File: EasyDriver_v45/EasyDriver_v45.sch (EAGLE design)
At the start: 43 parts, among them IC1 A3967SLB, IC2 V_REG_317SMD

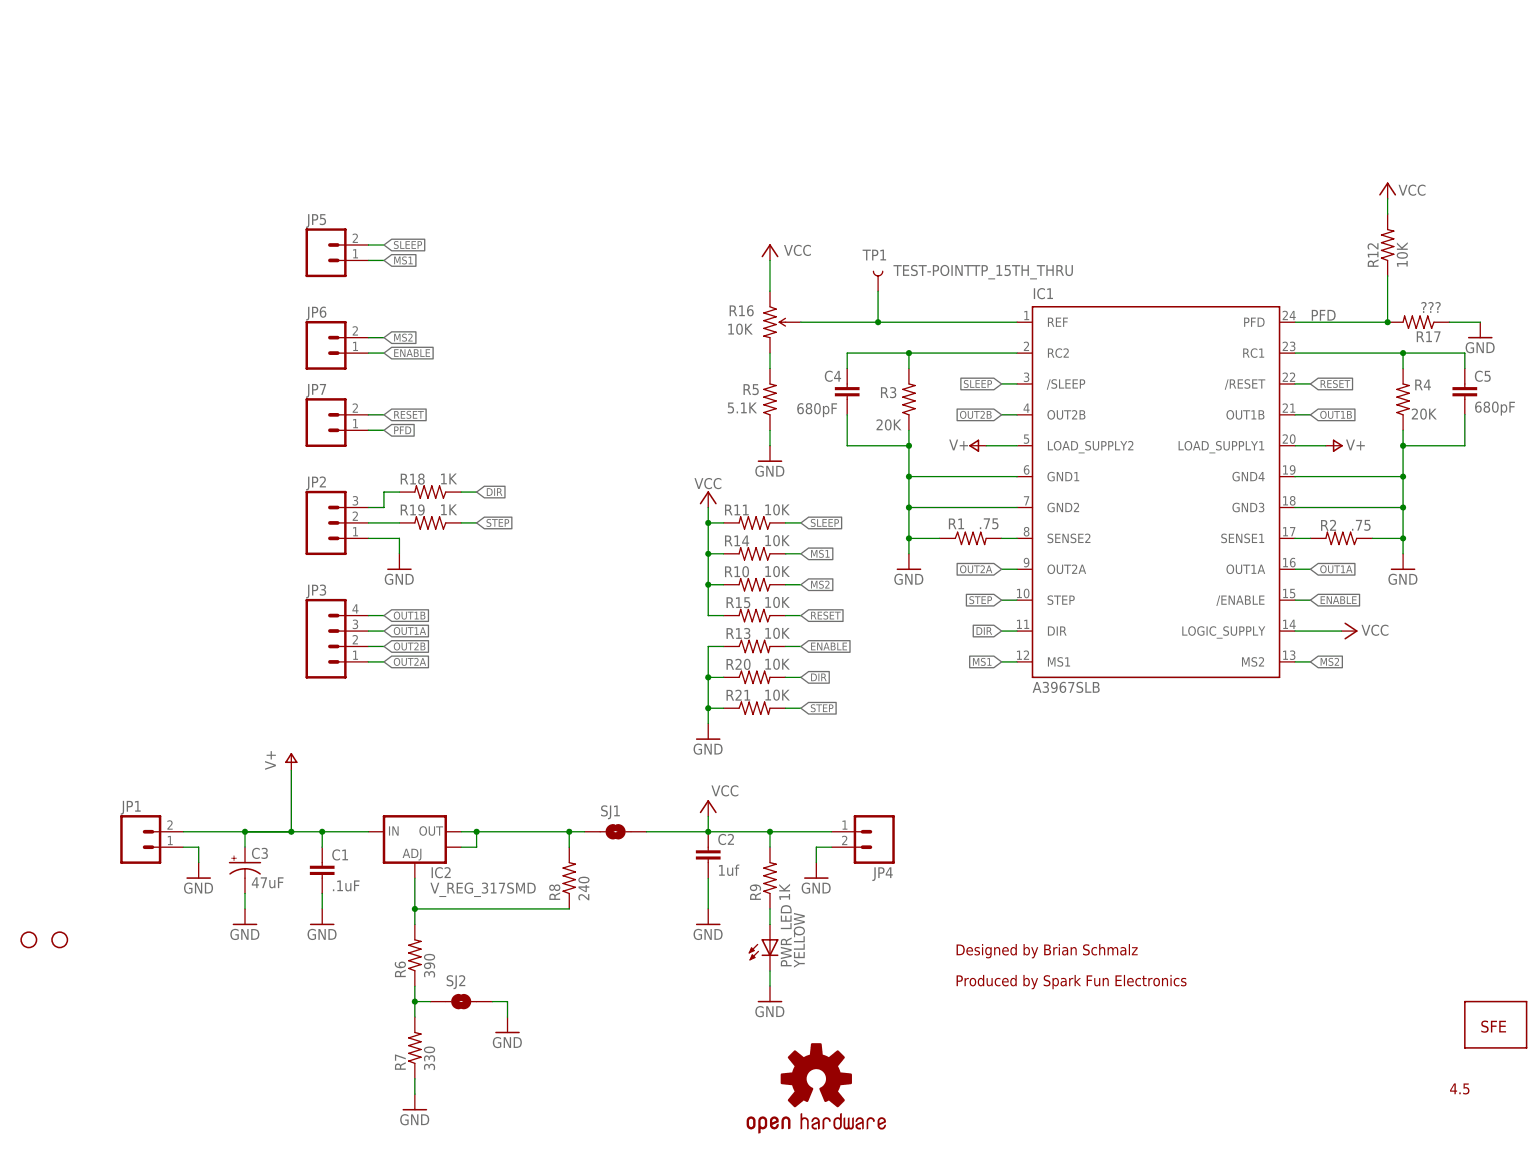
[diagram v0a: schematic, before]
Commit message: * Made TP1 bigger, and no longer covered with solder mask * Switched R5 to 2.4K Ohms to allow Vref down to 1V into driver * Set R17 to 6.8K to allow PFD input to select 'mixed-decay' mode * Swapped location of STEP and DIR series resistors so that pull downs now happen before series Rs. * Suggest SparkFun adjust current limit pot to 2V (measured by TP1) at final test.
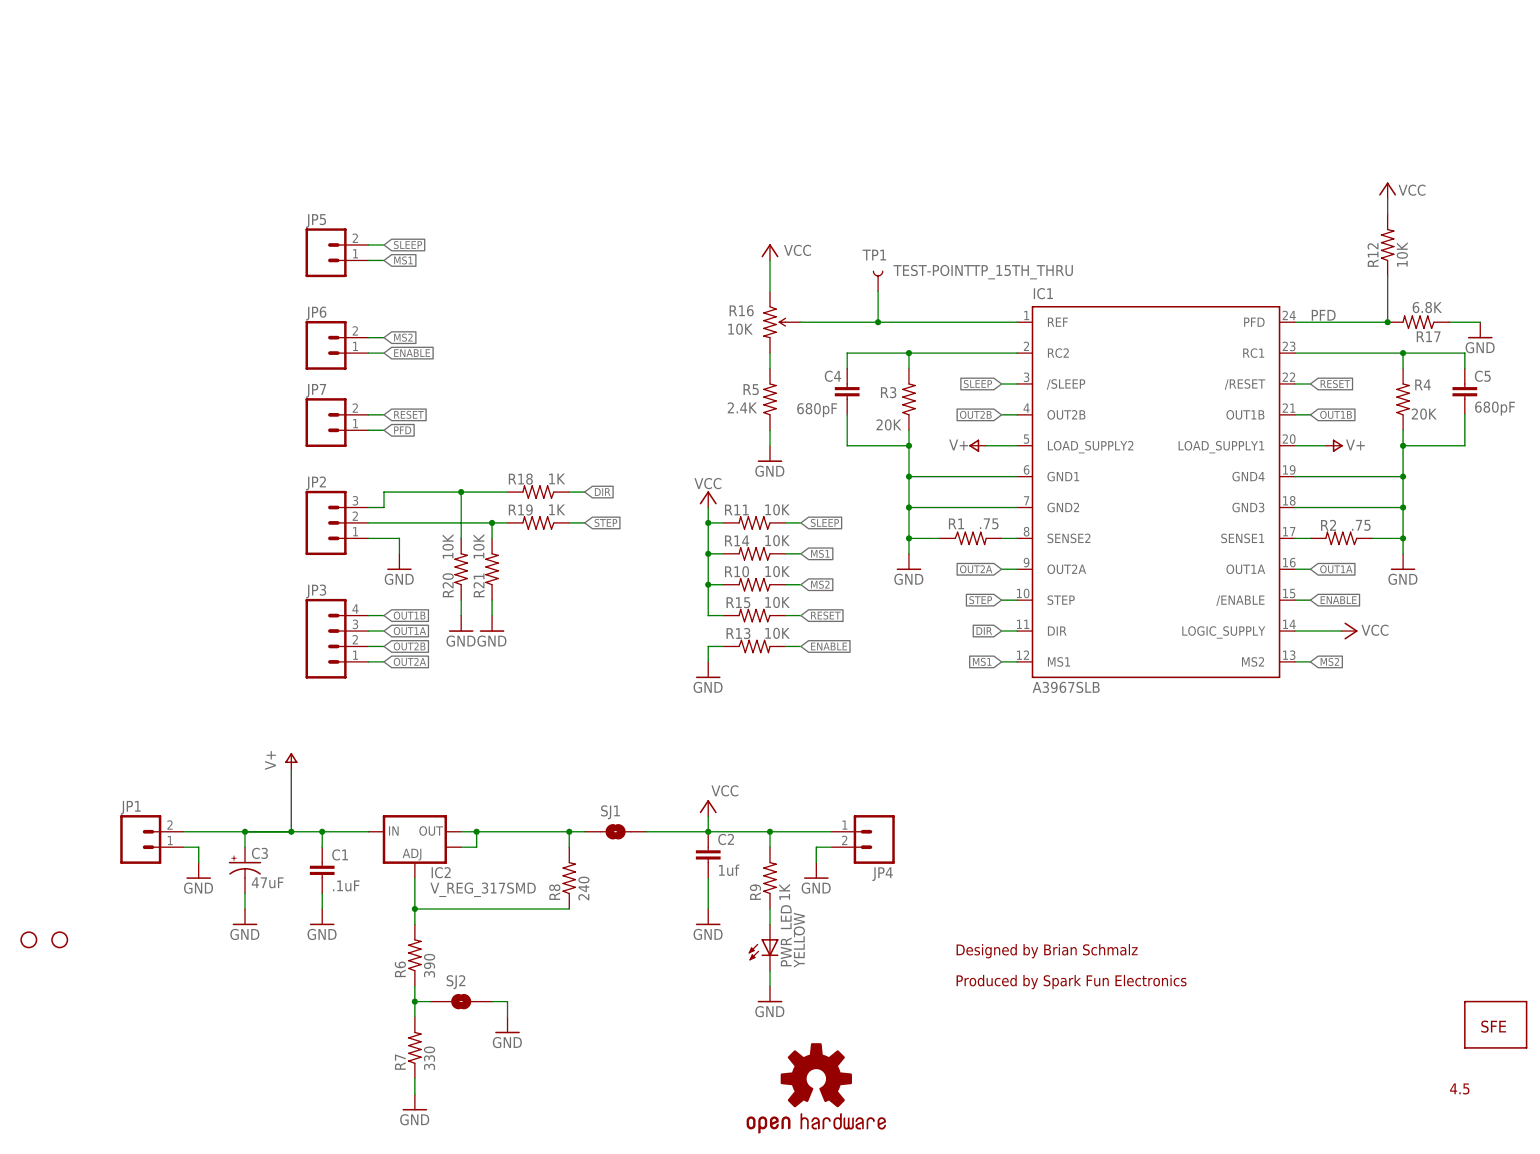
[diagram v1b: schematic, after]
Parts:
- R17: value ??? -> 6.8K
- R5: value 5.1K -> 2.4K
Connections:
- net N$12 renamed VREF
- net DIR: no longer R20.2
- net DIR_IN: now also R20.2
- net STEP: no longer R21.2
- net STEP_IN: now also R21.2
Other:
- note added: "Added series resistors and pull downs on STEP/DIR Updated pot fooprint Made bottom layer GND rather than VCC Updated to latest SparkFun footprints Swithed from CC BY 3.0 to CC BY-SA 3.0 license Fixed pot silkscreen direction R5 now 2.5K Ohms to get down to 1V on Vref R17 now 6.8K to set PDF to 'mixed-decay' mode"
- note added: "Set R16 to 2.0V at factory = 333mA/phase"
- note added: "Set for 'mixed-decay' mode."
- note removed: "Added series resistors and pull downs on STEP/DIR Updated pot fooprint Made bottom layer GND rather than VCC Updated to latest SparkFun footprints Swithed from CC BY 3.0 to CC BY-SA 3.0 license Fixed pot silkscreen direction"
- note removed: "Change R12 and add in"
- note removed: "NOPOP"
- note removed: "R17 to create any voltage"
- note removed: "See datasheet"
- note removed: "on PFD for best high"
- note removed: "speed performance."
- moved on the sheet: R18, R19, R20, R21

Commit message: Based on SparkFun feedback * Replaced frame with newest version from SparkFun library * Replaced VCC symbol with newest version from SparkFun library * Move components so that keepout area around mounding holes is honored.
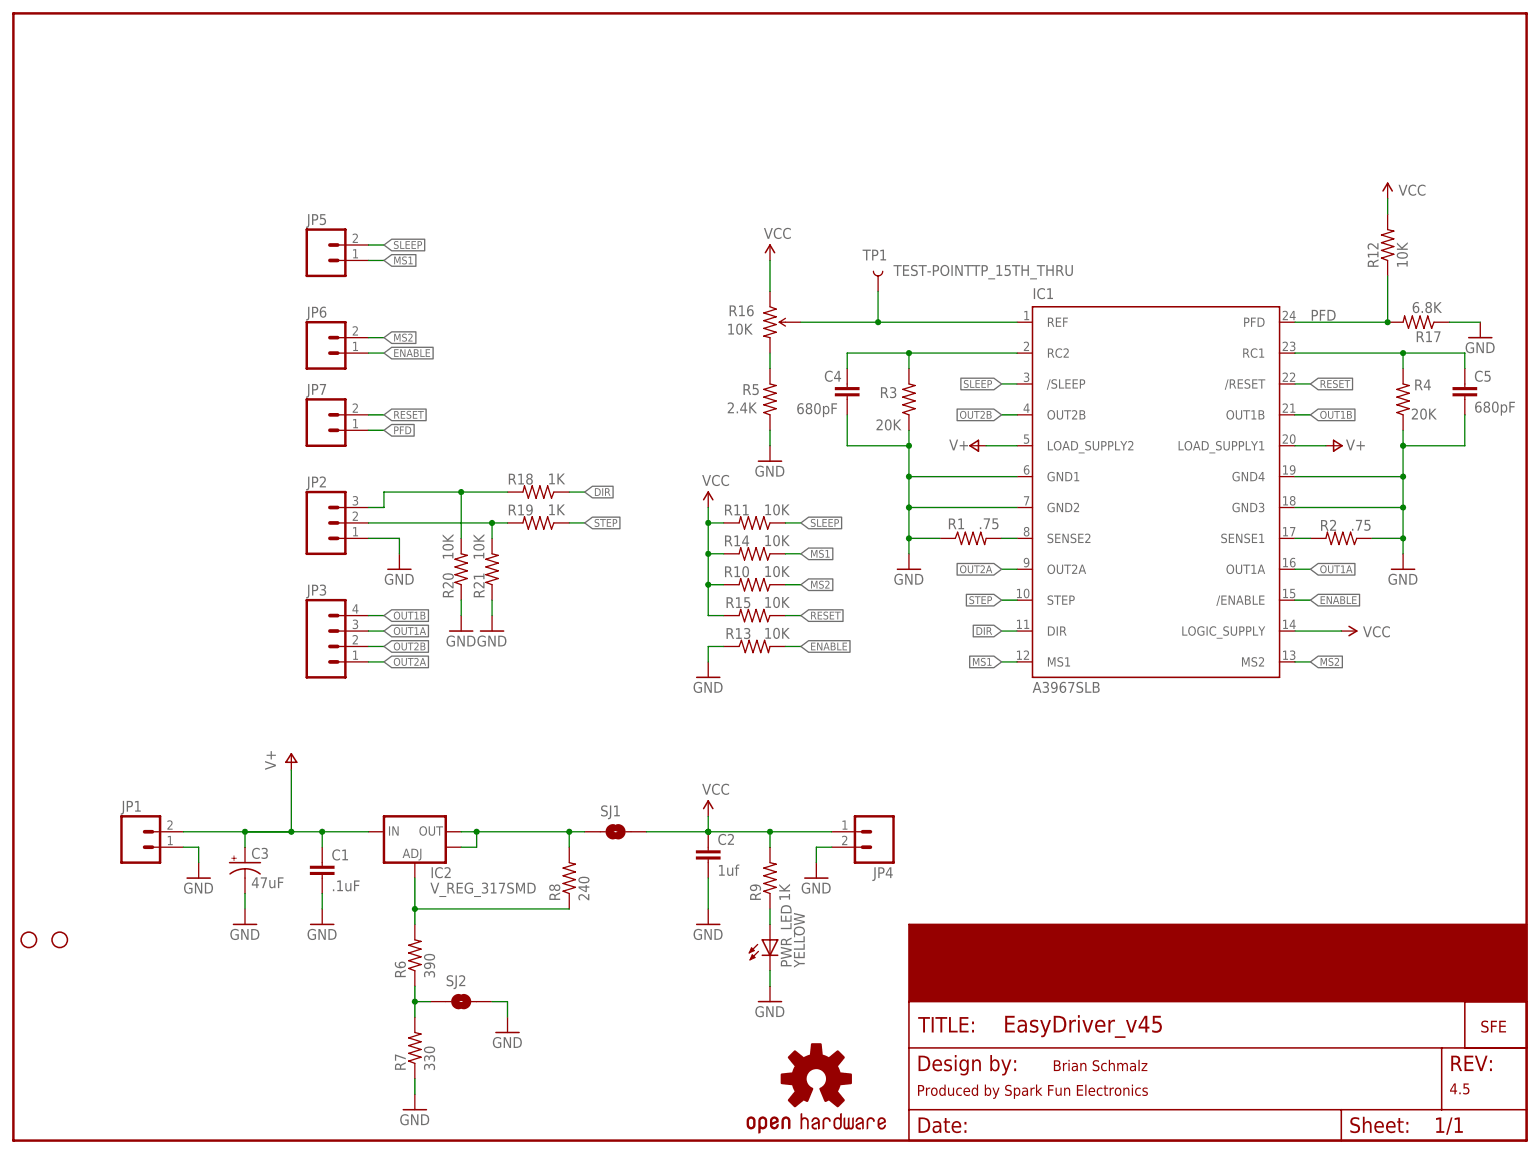
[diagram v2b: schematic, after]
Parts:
- added FRAME2: FRAME-LETTER, SparkFun-Aesthetics:FRAME-LETTER
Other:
- note added: "Brian Schmalz"
- note removed: "Designed by Brian Schmalz"
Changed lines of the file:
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@@
 <?xml version="1.0" encoding="utf-8"?>
 <!DOCTYPE eagle SYSTEM "eagle.dtd">
-<eagle version="6.4">
+<eagle version="6.5.0">
 <drawing>
 <settings>
@@
 <part name="GND2" library="supply1" deviceset="GND" device=""/>
 <part name="GND3" library="supply1" deviceset="GND" device=""/>
-<part name="P+3" library="supply1" deviceset="+5V" device="" value="VCC"/>
 <part name="GND6" library="supply1" deviceset="GND" device=""/>
-<part name="P+5" library="supply1" deviceset="+5V" device="" value="VCC"/>
 <part name="R1" library="SparkFun-Resistors" deviceset="RESISTOR" device="0805-RES" value=".75"/>
 <part name="R2" library="SparkFun-Resistors" deviceset="RESISTOR" device="0805-RES" value=".75"/>
@@
 <part name="R3" library="SparkFun-Resistors" deviceset="RESISTOR" device="0603" value="20K"/>
 <part name="C2" library="SparkFun-Capacitors" deviceset="CAP" device="0603-CAP" value="1uf"/>
-<part name="P+4" library="supply1" deviceset="+5V" device="" value="VCC"/>
 <part name="C3" library="rcl" deviceset="CPOL-US" device="D" value="47uF"/>
 <part name="P+10" library="supply1" deviceset="V+" device=""/>
 <part name="P+11" library="supply1" deviceset="V+" device=""/>
 <part name="MOT_PWR" library="supply1" deviceset="V+" device=""/>
-<part name="P+13" library="supply1" deviceset="+5V" device="" value="VCC"/>
 <part name="GND1" library="supply1" deviceset="GND" device=""/>
 <part name="R5" library="SparkFun-Resistors" deviceset="RESISTOR" device="0603" value="2.4K"/>
-<part name="FRAME1" library="SparkFun" deviceset="FRAME-LETTER" device=""/>
 <part name="R6" library="SparkFun-Resistors" deviceset="RESISTOR" device="0603" value="390"/>
 <part name="R8" library="SparkFun-Resistors" deviceset="RESISTOR" device="0603" value="240"/>
@@
 <part name="R15" library="SparkFun-Resistors" deviceset="RESISTOR" device="0603" value="10K"/>
 <part name="R10" library="SparkFun-Resistors" deviceset="RESISTOR" device="0603" value="10K"/>
-<part name="P+1" library="supply1" deviceset="+5V" device="" value="VCC"/>
 <part name="C4" library="SparkFun-Capacitors" deviceset="CAP" device="0603-CAP" value="680pF"/>
 <part name="C5" library="SparkFun-Capacitors" deviceset="CAP" device="0603-CAP" value="680pF"/>
@@
 <part name="GND8" library="supply1" deviceset="GND" device=""/>
 <part name="GND16" library="supply1" deviceset="GND" device=""/>
+<part name="FRAME2" library="SparkFun-Aesthetics" deviceset="FRAME-LETTER" device=""/>
+<part name="SUPPLY1" library="SparkFun-Aesthetics" deviceset="VCC" device=""/>
+<part name="SUPPLY2" library="SparkFun-Aesthetics" deviceset="VCC" device=""/>
+<part name="SUPPLY3" library="SparkFun-Aesthetics" deviceset="VCC" device=""/>
+<part name="SUPPLY4" library="SparkFun-Aesthetics" deviceset="VCC" device=""/>
+<part name="SUPPLY5" library="SparkFun-Aesthetics" deviceset="VCC" device=""/>
 </parts>
 <sheets>
 <sheet>
 <plain>
-<text x="154.94" y="30.48" size="1.778" layer="94">Designed by Brian Schmalz</text>
-<text x="154.94" y="25.4" size="1.778" layer="94">Produced by Spark Fun Electronics</text>
+<text x="170.942" y="11.43" size="1.778" layer="94">Brian Schmalz</text>
+<text x="148.59" y="7.366" size="1.778" layer="94">Produced by Spark Fun Electronics</text>
 <text x="134.62" y="55.88" size="1.778" layer="98">Vcc output
 Max 70mA used
@@
 <text x="116.84" y="154.94" size="1.778" layer="98">Max Coil Current(in Amps) = Vref(in Volts)/6</text>
 <text x="116.84" y="152.4" size="1.778" layer="98">Set R16 to 2.0V at factory = 333mA/phase</text>
+<rectangle x1="147.32" y1="22.86" x2="248.92" y2="35.56" layer="94"/>
 </plain>
 <instances>
@@
 <instance part="GND2" gate="1" x="147.32" y="93.98"/>
 <instance part="GND3" gate="1" x="228.6" y="93.98"/>
-<instance part="P+3" gate="1" x="220.98" y="83.82" smashed="yes" rot="R270">
-<attribute name="VALUE" x="221.742" y="83.058" size="1.778" layer="96"/>
-</instance>
 <instance part="GND6" gate="1" x="114.3" y="76.2"/>
-<instance part="P+5" gate="1" x="114.3" y="106.68" smashed="yes">
-<attribute name="VALUE" x="112.014" y="107.188" size="1.778" layer="96"/>
-</instance>
 <instance part="R1" gate="G$1" x="157.48" y="99.06" smashed="yes">
 <attribute name="NAME" x="153.67" y="100.5586" size="1.778" layer="95"/>
@@
 </instance>
 <instance part="C2" gate="G$1" x="114.3" y="45.72"/>
-<instance part="P+4" gate="1" x="114.3" y="55.88" smashed="yes">
-<attribute name="VALUE" x="114.808" y="56.642" size="1.778" layer="96"/>
-</instance>
 <instance part="C3" gate="G$1" x="38.1" y="45.72"/>
 <instance part="P+10" gate="1" x="157.48" y="114.3" smashed="yes" rot="R90">
@@
 </instance>
 <instance part="MOT_PWR" gate="1" x="45.72" y="63.5"/>
-<instance part="P+13" gate="1" x="226.06" y="157.48" smashed="yes">
-<attribute name="VALUE" x="227.838" y="155.448" size="1.778" layer="96"/>
-</instance>
 <instance part="GND1" gate="1" x="124.46" y="111.76"/>
 <instance part="R5" gate="G$1" x="124.46" y="121.92" smashed="yes" rot="R90">
@@
 <attribute name="VALUE" x="117.348" y="119.634" size="1.778" layer="96"/>
 </instance>
-<instance part="FRAME1" gate="G$1" x="0" y="0"/>
-<instance part="FRAME1" gate="G$2" x="147.32" y="0"/>
 <instance part="R6" gate="G$1" x="66.04" y="30.48" rot="R90"/>
 <instance part="R8" gate="G$1" x="91.44" y="43.18" rot="R90"/>
@@
 <attribute name="NAME" x="116.84" y="92.6846" size="1.778" layer="95"/>
 <attribute name="VALUE" x="123.444" y="92.71" size="1.778" layer="96"/>
-</instance>
-<instance part="P+1" gate="1" x="124.46" y="147.32" smashed="yes">
-<attribute name="VALUE" x="126.746" y="145.542" size="1.778" layer="96"/>
 </instance>
 <instance part="C4" gate="G$1" x="137.16" y="121.92" smashed="yes">
@@
 <instance part="GND8" gate="1" x="73.66" y="83.82"/>
 <instance part="GND16" gate="1" x="78.74" y="83.82"/>
+<instance part="FRAME2" gate="G$1" x="0" y="0"/>
+<instance part="FRAME2" gate="G$2" x="147.32" y="0"/>
+<instance part="SUPPLY1" gate="G$1" x="114.3" y="53.34"/>
+<instance part="SUPPLY2" gate="G$1" x="124.46" y="144.78"/>
+<instance part="SUPPLY3" gate="G$1" x="226.06" y="154.94" smashed="yes">
+<attribute name="VALUE" x="227.838" y="155.448" size="1.778" layer="96"/>
+</instance>
+<instance part="SUPPLY4" gate="G$1" x="218.44" y="83.82" smashed="yes" rot="R270">
+<attribute name="VALUE" x="221.996" y="82.804" size="1.778" layer="96"/>
+</instance>
+<instance part="SUPPLY5" gate="G$1" x="114.3" y="104.14"/>
 </instances>
 <busses>
@@
 <segment>
 <wire x1="226.06" y1="152.4" x2="226.06" y2="154.94" width="0.1524" layer="91"/>
-<pinref part="P+13" gate="1" pin="+5V"/>
 <pinref part="R12" gate="G$1" pin="2"/>
+<pinref part="SUPPLY3" gate="G$1" pin="VCC"/>
 </segment>
 <segment>
 <wire x1="210.82" y1="83.82" x2="218.44" y2="83.82" width="0.1524" layer="91"/>
 <pinref part="IC1" gate="G$1" pin="LOGIC_SUPPLY"/>
-<pinref part="P+3" gate="1" pin="+5V"/>
+<pinref part="SUPPLY4" gate="G$1" pin="VCC"/>
 </segment>
 <segment>
 <wire x1="116.84" y1="101.6" x2="114.3" y2="101.6" width="0.1524" layer="91"/>
-<wire x1="114.3" y1="101.6" x2="114.3" y2="104.14" width="0.1524" layer="91"/>
-<pinref part="P+5" gate="1" pin="+5V"/>
 <pinref part="R11" gate="G$1" pin="2"/>
 <wire x1="114.3" y1="96.52" x2="116.84" y2="96.52" width="0.1524" layer="91"/>
@@
 <wire x1="114.3" y1="86.36" x2="114.3" y2="91.44" width="0.1524" layer="91"/>
 <junction x="114.3" y="91.44"/>
-</segment>
-<segment>
+<pinref part="SUPPLY5" gate="G$1" pin="VCC"/>
+<wire x1="114.3" y1="101.6" x2="114.3" y2="104.14" width="0.1524" layer="91"/>
+</segment>
+<segment>
+<pinref part="R16" gate="R?" pin="CCW"/>
+<pinref part="SUPPLY2" gate="G$1" pin="VCC"/>
 <wire x1="124.46" y1="139.7" x2="124.46" y2="144.78" width="0.1524" layer="91"/>
-<pinref part="P+1" gate="1" pin="+5V"/>
-<pinref part="R16" gate="R?" pin="CCW"/>
-</segment>
-<segment>
-<wire x1="114.3" y1="53.34" x2="114.3" y2="50.8" width="0.1524" layer="91"/>
+</segment>
+<segment>
 <wire x1="134.62" y1="50.8" x2="124.46" y2="50.8" width="0.1524" layer="91"/>
 <wire x1="124.46" y1="50.8" x2="114.3" y2="50.8" width="0.1524" layer="91"/>
@@
 <junction x="114.3" y="50.8"/>
 <junction x="124.46" y="50.8"/>
-<pinref part="P+4" gate="1" pin="+5V"/>
 <pinref part="C2" gate="G$1" pin="1"/>
 <pinref part="R9" gate="G$1" pin="2"/>
 <pinref part="SJ1" gate="1" pin="2"/>
 <pinref part="JP4" gate="G$1" pin="1"/>
+<pinref part="SUPPLY1" gate="G$1" pin="VCC"/>
+<wire x1="114.3" y1="53.34" x2="114.3" y2="50.8" width="0.1524" layer="91"/>
+<junction x="114.3" y="50.8"/>
 </segment>
 </net>
